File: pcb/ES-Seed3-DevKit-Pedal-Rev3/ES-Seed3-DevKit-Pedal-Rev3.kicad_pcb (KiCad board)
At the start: 2 copper layers, 197 x 100 mm, 151 parts, among them J1 DIN_MIDI_5P, J10 DIN_MIDI_5P, J11 DIN_MIDI_5P, J2 JACK_TRS_SWITCHING, J3 JACK_TRS_SWITCHING, J4 JACK_TRS_SWITCHING, J5 JACK_TRS_SWITCHING, J6 JACK_TRS_SWITCHING, J7 USB4110GFA, J8 Barrel_Jack_Switch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

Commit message: first review/prod folders after making all changes.
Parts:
- added QR1: ~, shnsly:qr-seed3-pedal-redirect-medium, F.Cu at (151.0, 124.5)
- VR1, VR2, VR3, VR4, VR5, VR6: value P-10K-B-R-PIP -> P-10K-B-R
- moved C24 2.60 mm to (154.6, 84.5)
- moved R48 2.60 mm to (175.6, 79.7)
- moved R55 2.60 mm to (166.8, 79.7)
- moved C13 2.50 mm to (180.0, 84.5)
- moved C14 2.50 mm to (171.3, 84.5)
- moved C23 2.50 mm to (162.6, 84.5)
- moved R46 0.60 mm to (218.7, 81.6)
- moved R59 0.60 mm to (227.2, 81.6)
- moved R61 0.60 mm to (224.4, 81.6)
- moved R68 0.60 mm to (221.6, 81.6)
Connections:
- A1 pad 12: unconnected-(A1-I2C1_SCL-Pad12) -> SDMMC_DETECT
- J2 pad R: (no net) -> unconnected-(J2-PadR)
- J2 pad RN: (no net) -> unconnected-(J2-PadRN)
- J2 pad S: (no net) -> GND
- J2 pad SN: (no net) -> unconnected-(J2-PadSN)
- J2 pad T: (no net) -> AUDIO_IN_LEFT
- J2 pad TN: (no net) -> Net-(J2-PadTN)
- J3 pad R: (no net) -> unconnected-(J3-PadR)
- J3 pad RN: (no net) -> unconnected-(J3-PadRN)
- J3 pad S: (no net) -> GND
- J3 pad SN: (no net) -> unconnected-(J3-PadSN)
- J3 pad T: (no net) -> AUDIO_OUT_LEFT
- J3 pad TN: (no net) -> unconnected-(J3-PadTN)
- J4 pad R: (no net) -> unconnected-(J4-PadR)
- J4 pad RN: (no net) -> unconnected-(J4-PadRN)
- J4 pad S: (no net) -> GND
- J4 pad SN: (no net) -> unconnected-(J4-PadSN)
- J4 pad T: (no net) -> AUDIO_IN_RIGHT
- J4 pad TN: (no net) -> Net-(J4-PadTN)
- J5 pad R: (no net) -> unconnected-(J5-PadR)
- J5 pad RN: (no net) -> unconnected-(J5-PadRN)
- J5 pad S: (no net) -> GND
- J5 pad SN: (no net) -> unconnected-(J5-PadSN)
- J5 pad T: (no net) -> AUDIO_OUT_RIGHT
- J5 pad TN: (no net) -> unconnected-(J5-PadTN)
- J6 pad R: (no net) -> Net-(J6-PadR)
- J6 pad RN: (no net) -> unconnected-(J6-PadRN)
- J6 pad S: (no net) -> GND
- J6 pad SN: (no net) -> unconnected-(J6-PadSN)
- J6 pad T: (no net) -> EXPRESSION_IN_EXT
- J6 pad TN: (no net) -> Net-(J6-PadTN)
- R46 pad 1: Net-(J6-RING) -> Net-(J6-PadR)
- R64 pad 2: Net-(J2-TIP_SW) -> Net-(J2-PadTN)
- R65 pad 2: Net-(J4-TIP_SW) -> Net-(J4-PadTN)
- R68 pad 2: Net-(J6-TIP_SW) -> Net-(J6-PadTN)
- U7 pad CD1: unconnected-(U7-CD-PadCD1) -> SDMMC_DETECT
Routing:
- net SDMMC_DETECT: track 0.00 -> 76.3 mm, vias 0 -> 3
- net Net-(J6-PadR): track 0.00 -> 26.3 mm
- net Net-(J6-RING): track 25.7 -> 0.00 mm
- net Net-(J6-PadTN): track 0.00 -> 8.12 mm
- net Net-(J6-TIP_SW): track 7.52 -> 0.00 mm
- net Net-(J4-TIP_SW): track 3.86 -> 0.00 mm
- net Net-(J4-PadTN): track 0.00 -> 3.86 mm
- net Net-(J2-TIP_SW): track 3.78 -> 0.00 mm
- net Net-(J2-PadTN): track 0.00 -> 3.78 mm
- net +9V: track 141.4 -> 144.3 mm
- net +9V_A: track 196.8 -> 199.0 mm
- net Net-(J11-4): track 12.3 -> 12.9 mm
- net +5V_A: track 171.9 -> 171.3 mm
- net +3V3: track 289.3 -> 288.7 mm
- net GND: vias 0 -> 4

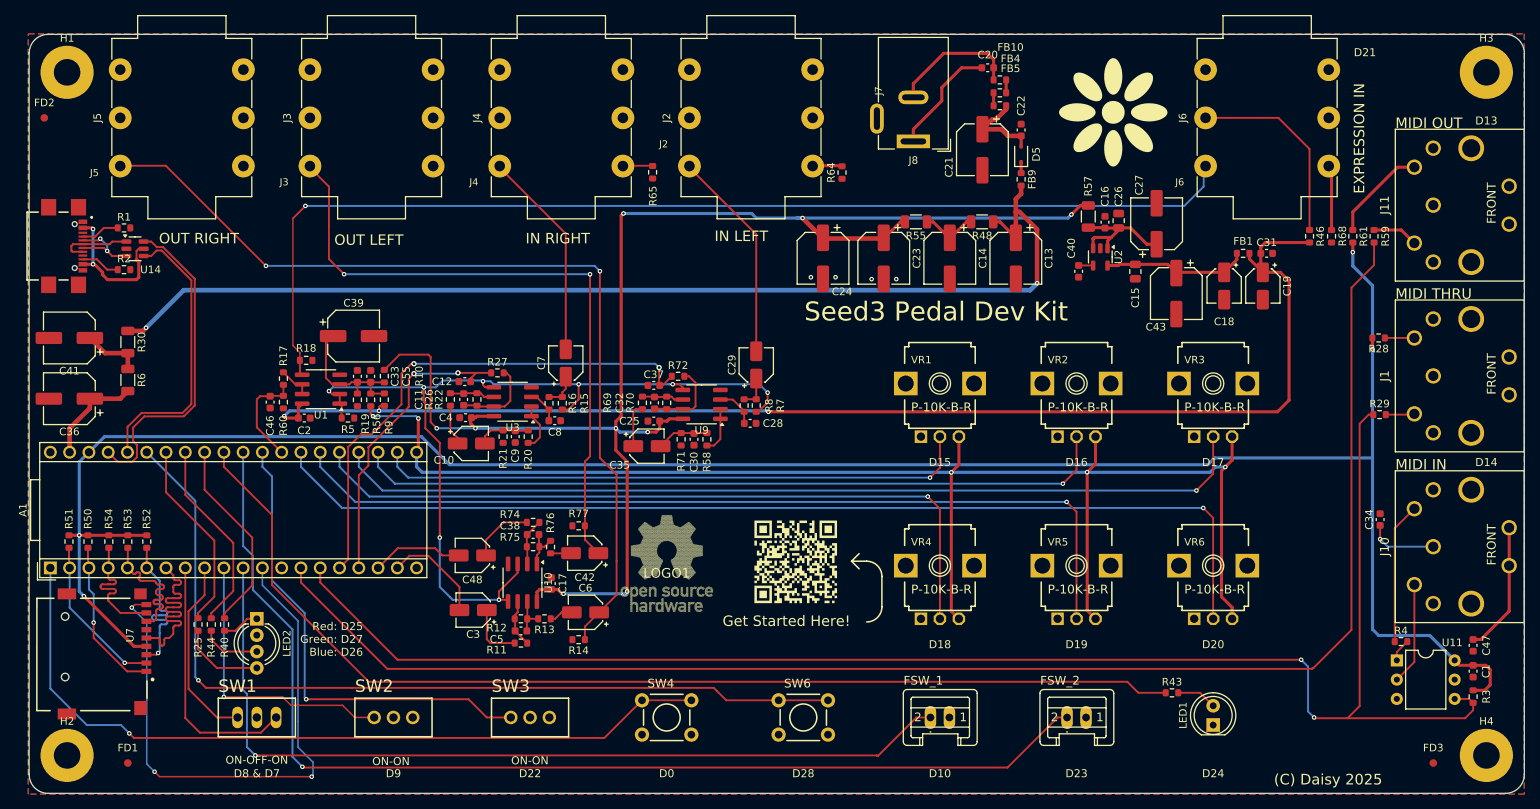
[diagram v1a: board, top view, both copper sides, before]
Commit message: boxes around daisy pins, osh logo fix, etc.
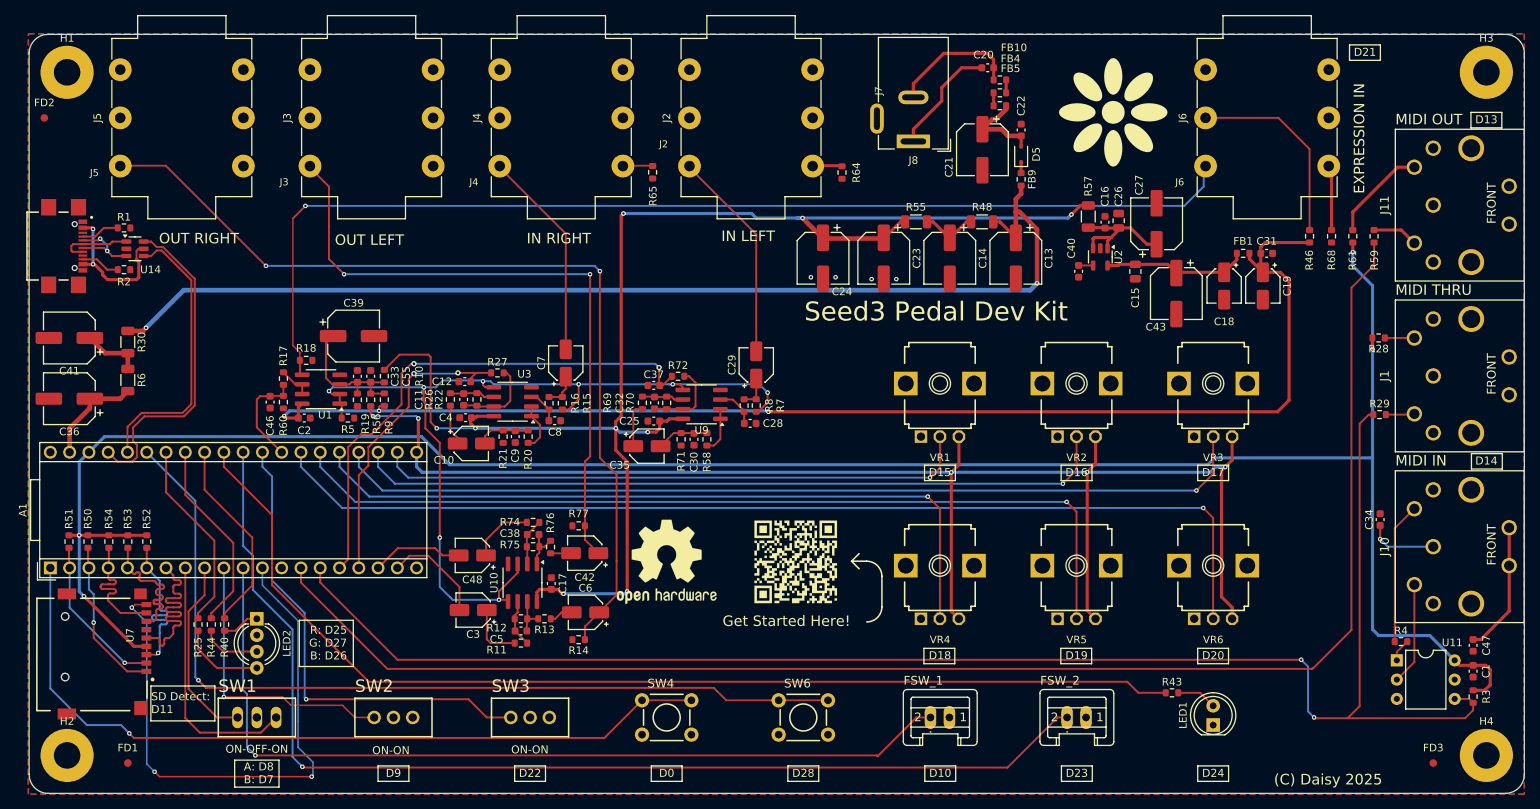
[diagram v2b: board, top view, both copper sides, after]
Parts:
- LOGO1: footprint parts-for-kicad:OSHW-LOGO-L_TEXT -> Symbol:OSHW-Logo2_14.6x12mm_SilkScreen
- QR1: footprint shnsly:qr-seed3-pedal-redirect-medium -> shnsly:qr-seed3-desktop-redirect-medium
- moved LOGO1 1.51 mm to (134.0, 124.5)
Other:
- board text added: "A: D8 B: D7"
- board text added: "R: D25 G: D27 B: D26"
- board text added: "SD Detect: D11"
- board text removed: "D8 & D7"
- board text removed: "Red: D25 Green: D27 Blue: D26"

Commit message: prod mats with last bits of silk adjustment.
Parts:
- renumbered SW6 to SW5
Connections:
- net TAC_SW1 renamed TAC_SW4
- net TAC_SW2 renamed TAC_SW5
- net TOG_1 renamed TOG_SW2
- net TOG_2_A renamed TOG_SW1_A
- net TOG_2_B renamed TOG_SW1_B
- net TOG_3 renamed TOG_SW3
